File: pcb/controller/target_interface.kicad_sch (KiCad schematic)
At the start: 2 parts, among them J1 Conn_01x06, J2 Pogo_01x06_male

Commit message: cleaned up
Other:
- note added: "Resistor Values not final!"
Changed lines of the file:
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@@
 	(generator_version "9.0")
 	(paper "A4")
+	(text "Resistor Values not final!"
+		(exclude_from_sim no)
+		(at 52.324 68.072 0)
+		(effects
+			(font
+				(size 1.27 1.27)
+			)
+		)
+	)
 	(junction
 		(at 120.65 34.29)

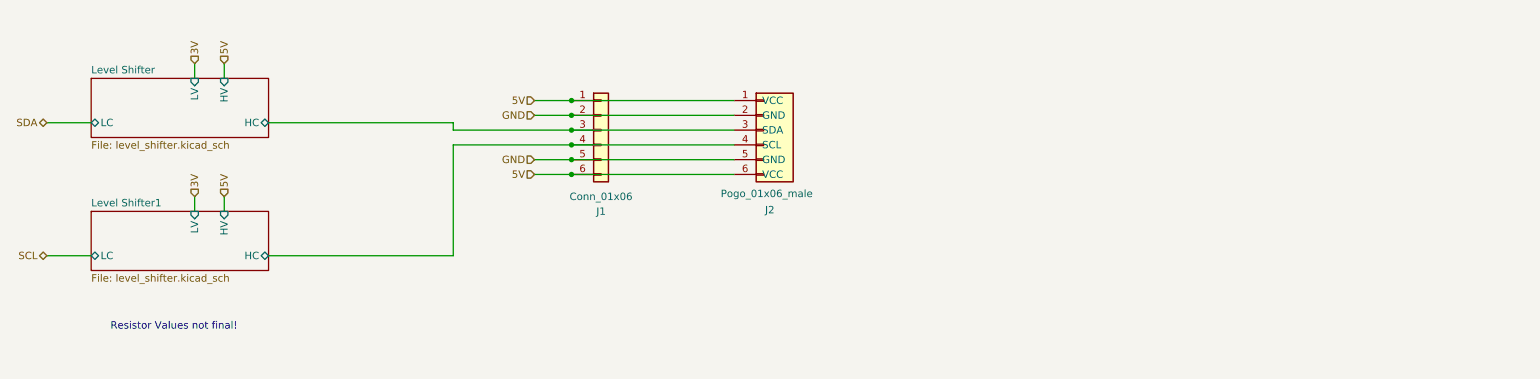
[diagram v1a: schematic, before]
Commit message: added lcsc numbers to all components and added ESD protection
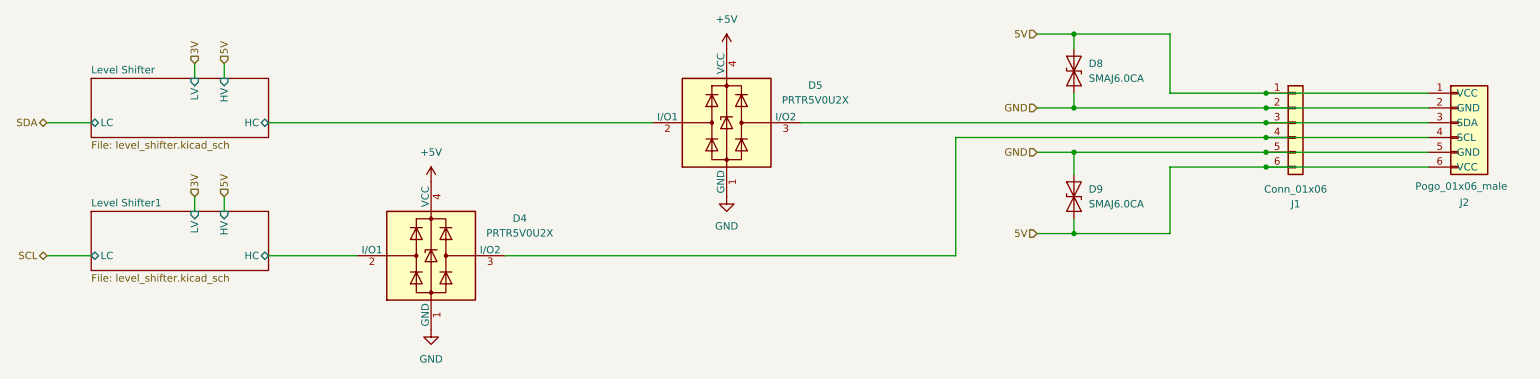
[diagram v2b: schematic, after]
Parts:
- added D4, D5: PRTR5V0U2X, Package_TO_SOT_SMD:SOT-143, symbol Power_Protection:PRTR5V0U2X
- added D8, D9: SMAJ6.0CA, Diode_SMD:D_SMA, symbol Diode:SMAJ6.0CA
- J2: footprint (none) -> external_footprints.petty:01x06 SMD 4x4mm pad
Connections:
- net 5V: now also D8.2 (A2), D9.1 (A1)
- net GND: now also D4.1 (GND), D5.1 (GND), D8.1 (A1), D9.2 (A2)
- net Level Shifter/HC: now also D5.2 (I/O1); no longer J1.3 (Pin_3), J2.3 (SDA)
- net Level Shifter1/HC: now also D4.2 (I/O1); no longer J1.4 (Pin_4), J2.4 (SCL)
- new net: D4.3 (I/O2), J1.4 (Pin_4), J2.4 (SCL)
- new net: D5.3 (I/O2), J1.3 (Pin_3), J2.3 (SDA)
- new net +5V: D4.4 (VCC), D5.4 (VCC)
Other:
- note removed: "Resistor Values not final!"
- moved on the sheet: J1, J2

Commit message: finished all pcbs by adjusting traces acording to 1oz copper weight
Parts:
- J1, J2: now left out of the parts list
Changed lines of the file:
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@@
 		(unit 1)
 		(exclude_from_sim no)
-		(in_bom yes)
+		(in_bom no)
 		(on_board yes)
 		(dnp no)
@@
 		(unit 1)
 		(exclude_from_sim no)
-		(in_bom yes)
-		(on_board yes)
-		(dnp no)
+		(in_bom no)
+		(on_board yes)
+		(dnp no)
